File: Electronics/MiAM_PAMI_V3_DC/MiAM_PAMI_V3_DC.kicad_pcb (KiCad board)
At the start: 2 copper layers, 62 x 95 mm, 28 parts, among them J1 TCRT5000L_Breakout, J2 Conn_01x03_Male, J3 SSD1306_vertical, J4 TCRT5000L_Breakout, J5 TCRT5000L_Breakout, J8 Conn_01x02_Pin, SW1 SW_DPDT_x2, U1 ESP32-DEVKITC-32U, U2 5V, U3 MT3608, U4 5V, U6 TB6612FNG

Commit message: Fix PCB
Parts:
- removed D2: D_Schottky, Diode_SMD:D_SOD-323_HandSoldering
- U2: value 5V -> 3V3
- moved BAT1 1.97 mm to (168.9, 55.3), turned to 90 degrees
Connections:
- BAT1 pad 1: /BATTERY_INPUT -> GND
- BAT1 pad 2: GND -> /BATTERY_INPUT
- U1 pad 19: Net-(D2-K) -> unconnected-(U1-EXT_5V-Pad19)
- U2 pad 1: /5V_BOARD -> +3V3
- U4 pad 3: /EMERGENCY_BUTTON -> +12V
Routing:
- net +3V3: track 184.8 -> 224.2 mm, vias 2 -> 4
- net /EMERGENCY_BUTTON: track 83.3 -> 44.1 mm
- net +12V: track 24.0 -> 39.3 mm
- net Net-(D2-K): track 4.98 -> 0.00 mm
- net /5V_BOARD: track 4.37 -> 0.00 mm
- net /BAT_READING: track 25.2 -> 22.3 mm
- net /ENCODER_B2: track 47.4 -> 49.1 mm
- net /BATTERY_INPUT: track 24.1 -> 25.4 mm
- net /TCRT1: track 66.8 -> 67.8 mm
- net /TCRT0: track 77.3 -> 78.3 mm
- net /TCRT2: track 58.4 -> 57.5 mm
- net /STBY: track 51.6 -> 50.8 mm

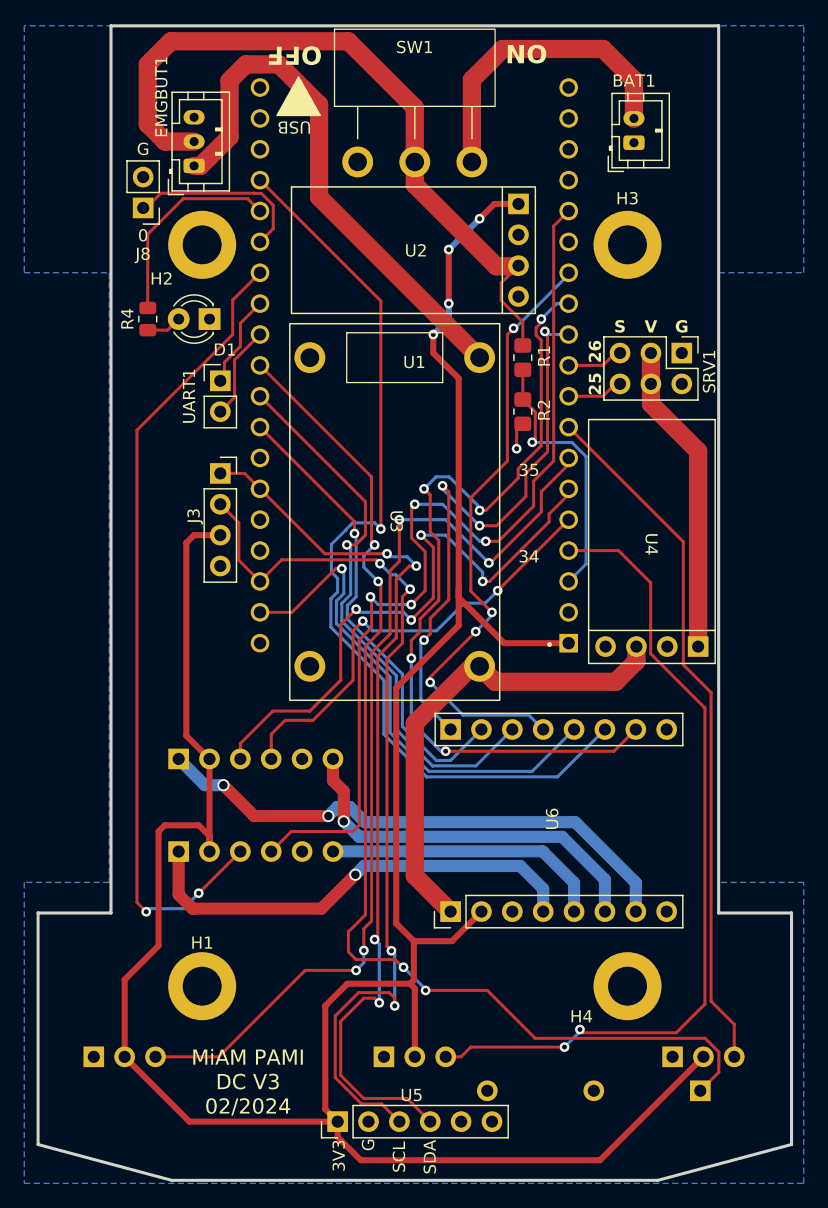
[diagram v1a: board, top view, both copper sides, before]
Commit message: Fix DC PAMI schematic
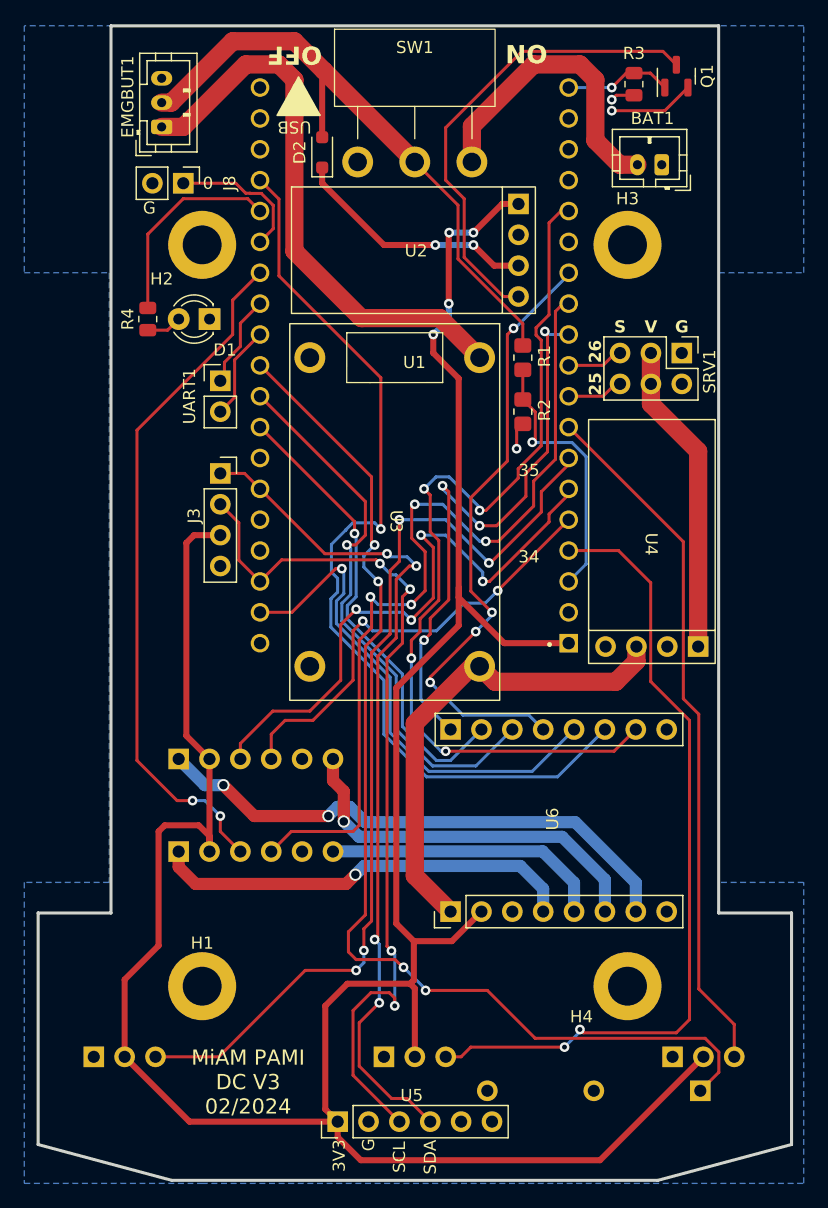
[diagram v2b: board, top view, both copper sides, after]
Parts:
- added D2: D_Schottky, Diode_SMD:D_SOD-323_HandSoldering, F.Cu at (143.3, 56.1)
- added Q1: BS170F, Package_TO_SOT_SMD:SOT-23, F.Cu at (172.4, 49.9)
- added R3: 50k, Resistor_SMD:R_0805_2012Metric, F.Cu at (168.9, 50.5)
- moved EMGBUT1 4.17 mm to (130.0, 54.0)
- moved J8 3.88 mm to (131.8, 58.7), turned to -90 degrees
- moved BAT1 2.92 mm to (171.2, 57.1), turned to 180 degrees
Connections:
- U1 pad 12: /EN34 -> /ENCODER_A1
- U1 pad 15: /ENCODER_A1 -> /EN34
- U1 pad 19: unconnected-(U1-EXT_5V-Pad19) -> /EXT_5V
- U2 pad 3: /POWER_SWITCH -> Net-(D2-K)
- U2 pad 4: unconnected-(U2-EN-Pad4) -> Net-(Q1-D)
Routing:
- net Net-(Q1-D): track 0.00 -> 39.1 mm
- net Net-(D2-K): track 0.00 -> 20.3 mm, vias 0 -> 2
- net /ENCODER_B1: track 66.9 -> 56.7 mm
- net GND: track 2.26 -> 11.3 mm, vias 1 -> 3
- net /EXT_5V: track 0.00 -> 8.90 mm, vias 0 -> 1
- net /POWER_SWITCH: track 59.9 -> 51.4 mm
- net /EN34: track 68.4 -> 75.8 mm, vias 5 -> 4
- net /ENCODER_A1: track 78.0 -> 70.8 mm
- net /SDA: track 74.7 -> 70.8 mm
- net /GPIO0: track 14.8 -> 11.0 mm
- net /1Y: track 38.1 -> 35.1 mm
- net /SCL: track 75.5 -> 72.7 mm
- net /EMERGENCY_BUTTON: track 44.1 -> 46.5 mm
- net /TCRT1: track 67.8 -> 66.8 mm
- net +3V3: track 224.2 -> 225.0 mm
